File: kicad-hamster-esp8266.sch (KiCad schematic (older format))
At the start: 16 parts

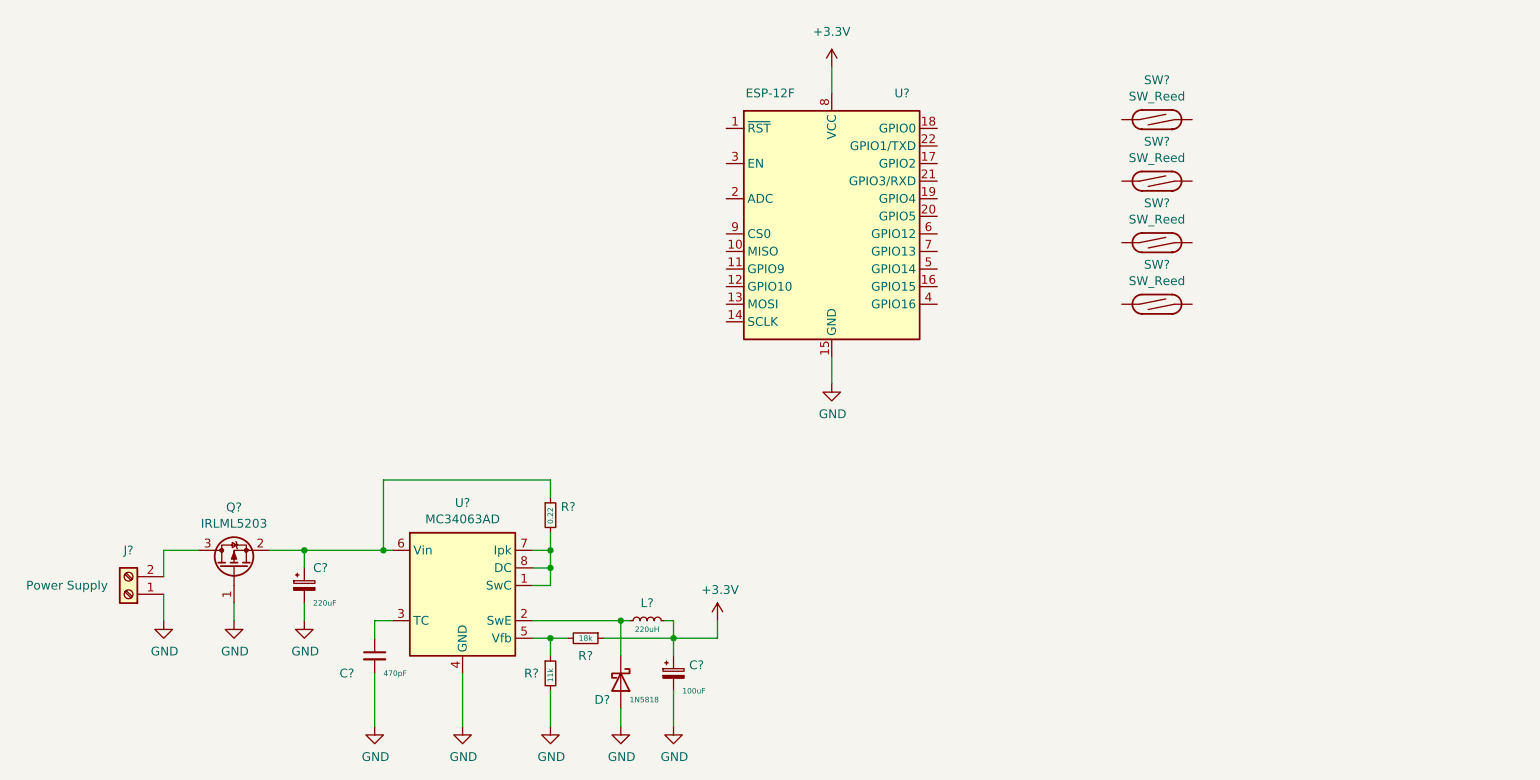
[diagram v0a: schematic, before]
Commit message: hamster v2 esp8266: flash/reset circuitry
Draw flash/reset/enable circuitry including control pins and
specific gpio pins.

Signed-off-by: Sergey Matyukevich <geomatsi@gmail.com>
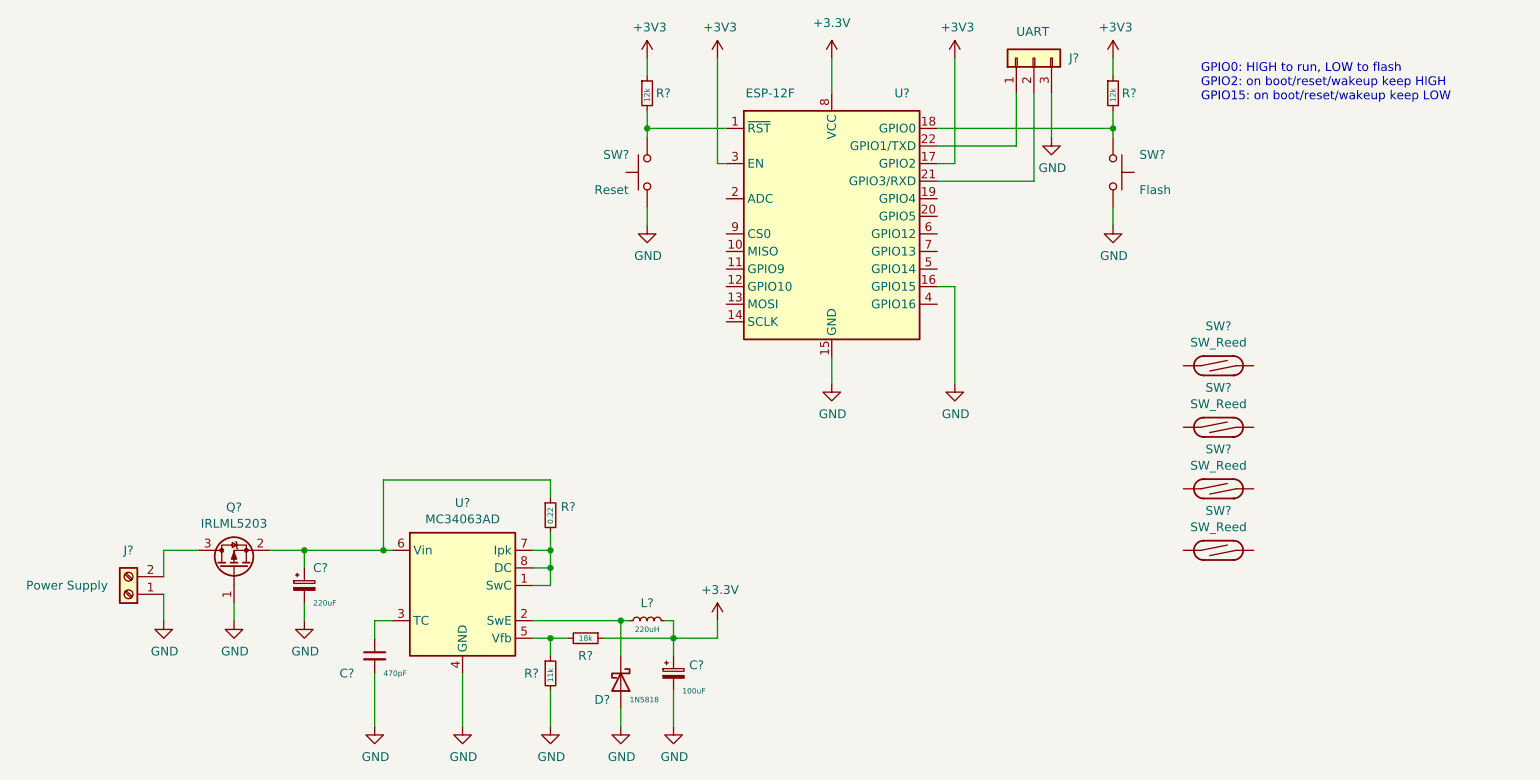
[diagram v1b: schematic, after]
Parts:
- added J?: UART, symbol Connector_Generic:Conn_01x03
- added R? (x2): 12k, symbol Device:R_Small
- added SW?: Flash, symbol Switch:SW_Push
- added SW?: Reset, symbol Switch:SW_Push
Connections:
- net +3V3: now also U?.17 (GPIO2), U?.3 (EN), R?.1, R?.1
- net GND: now also U?.16 (GPIO15), J?.3 (Pin_3), SW?.1, SW?.2
- net at U?.1 (~RST): now also R?.2, SW?.2
- net at U?.18 (GPIO0): now also R?.2, SW?.1
- net at U?.21 (GPIO3/RXD): now also J?.2 (Pin_2)
- net at U?.22 (GPIO1/TXD): now also J?.1 (Pin_1)
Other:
- note added: "GPIO0: HIGH to run, LOW to flash\nGPIO2: on boot/reset/wakeup keep HIGH\nGPIO15: on boot/reset/wakeup keep LOW"
- moved on the sheet: SW?

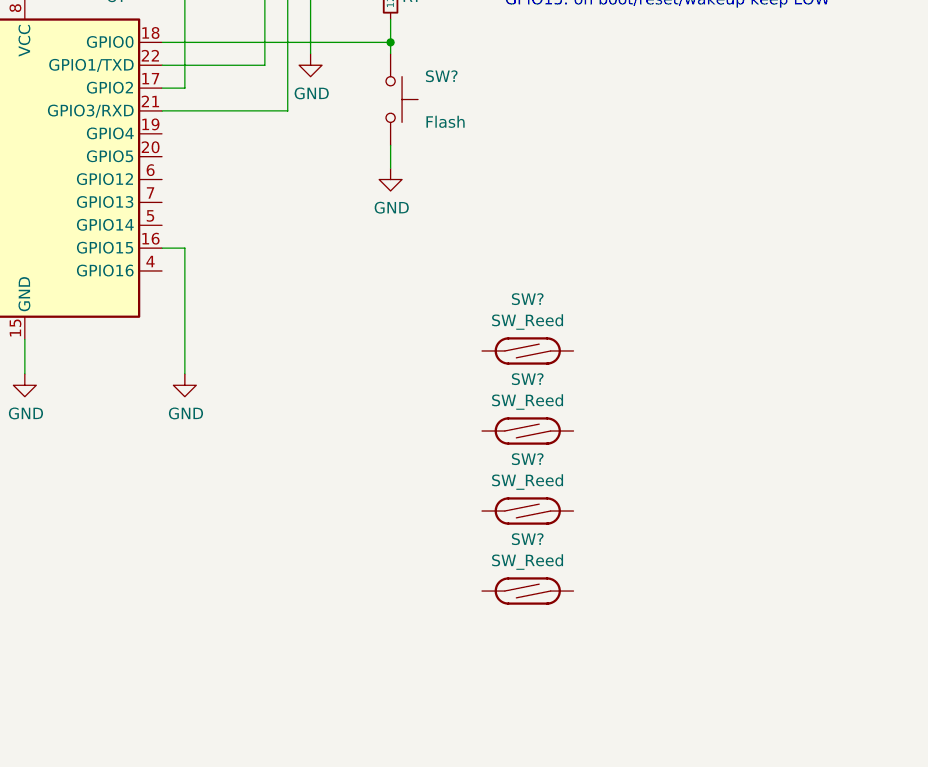
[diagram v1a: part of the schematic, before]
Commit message: hamster v2 esp8266: reed switch circuitry
Draw reed switch circuitry

Signed-off-by: Sergey Matyukevich <geomatsi@gmail.com>
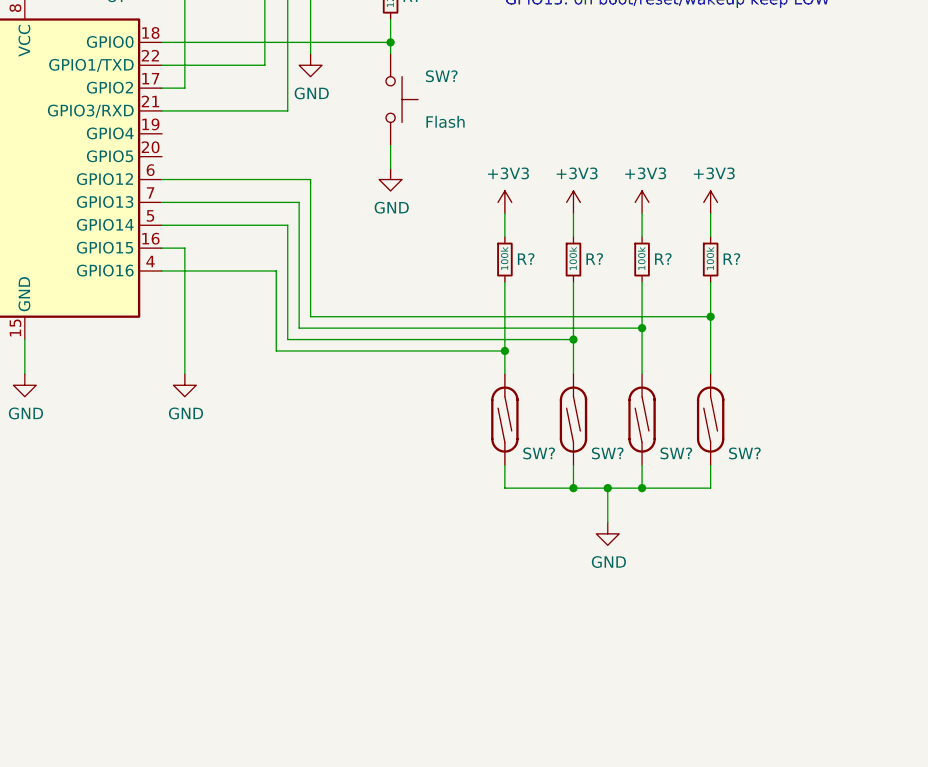
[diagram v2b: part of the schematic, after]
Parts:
- added R? (x4): 100k, symbol Device:R_Small
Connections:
- net +3V3: now also R?.1, R?.1, R?.1, R?.1
- net GND: now also SW?.1, SW?.1, SW?.1, SW?.1
- net at U?.4 (GPIO16): now also SW?.2, R?.2
- net at U?.5 (GPIO14): now also SW?.2, R?.2
- net at U?.6 (GPIO12): now also SW?.2, R?.2
- net at U?.7 (GPIO13): now also SW?.2, R?.2
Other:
- moved on the sheet: SW?
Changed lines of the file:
@@
 L Switch:SW_Reed SW?
 U 1 1 5F0BB0DF
-P 7700 5100
-F 0 "SW?" H 7700 5325 50  0000 C CNN
-F 1 "SW_Reed" H 7700 5232 50  0000 C CNN
-F 2 "" H 7700 5100 50  0001 C CNN
-F 3 "~" H 7700 5100 50  0001 C CNN
-	1    7700 5100
-	1    0    0    -1
+P 8500 4350
+F 0 "SW?" V 8350 4200 50  0000 C CNN
+F 1 "SW_Reed" H 8500 4482 50  0001 C CNN
+F 2 "" H 8500 4350 50  0001 C CNN
+F 3 "~" H 8500 4350 50  0001 C CNN
+	1    8500 4350
+	0    -1   -1   0
 $EndComp
 $Comp
 L Switch:SW_Reed SW?
 U 1 1 5F0BBD95
-P 7700 4750
-F 0 "SW?" H 7700 4975 50  0000 C CNN
-F 1 "SW_Reed" H 7700 4882 50  0000 C CNN
-F 2 "" H 7700 4750 50  0001 C CNN
-F 3 "~" H 7700 4750 50  0001 C CNN
-	1    7700 4750
-	1    0    0    -1
+P 8200 4350
+F 0 "SW?" V 8050 4200 50  0000 C CNN
+F 1 "SW_Reed" H 8200 4482 50  0001 C CNN
+F 2 "" H 8200 4350 50  0001 C CNN
+F 3 "~" H 8200 4350 50  0001 C CNN
+	1    8200 4350
+	0    -1   -1   0
 $EndComp
 $Comp
 L Switch:SW_Reed SW?
 U 1 1 5F0BC4C3
-P 7700 4400
-F 0 "SW?" H 7700 4625 50  0000 C CNN
-F 1 "SW_Reed" H 7700 4532 50  0000 C CNN
-F 2 "" H 7700 4400 50  0001 C CNN
-F 3 "~" H 7700 4400 50  0001 C CNN
-	1    7700 4400
-	1    0    0    -1
+P 7900 4350
+F 0 "SW?" V 7750 4200 50  0000 C CNN
+F 1 "SW_Reed" H 7900 4482 50  0001 C CNN
+F 2 "" H 7900 4350 50  0001 C CNN
+F 3 "~" H 7900 4350 50  0001 C CNN
+	1    7900 4350
+	0    -1   -1   0
 $EndComp
 $Comp
 L Switch:SW_Reed SW?
 U 1 1 5F0BCC12
-P 7700 4050
-F 0 "SW?" H 7700 4275 50  0000 C CNN
-F 1 "SW_Reed" H 7700 4182 50  0000 C CNN
-F 2 "" H 7700 4050 50  0001 C CNN
-F 3 "~" H 7700 4050 50  0001 C CNN
-	1    7700 4050
-	1    0    0    -1
+P 7600 4350
+F 0 "SW?" V 7450 4200 50  0000 C CNN
+F 1 "SW_Reed" H 7600 4482 50  0001 C CNN
+F 2 "" H 7600 4350 50  0001 C CNN
+F 3 "~" H 7600 4350 50  0001 C CNN
+	1    7600 4350
+	0    -1   -1   0
 $EndComp
 $Comp
@@
 Wire Wire Line
 	4850 2900 4850 2300
+$Comp
+L power:+3V3 #PWR?
+U 1 1 5F135AC7
+P 7900 3450
+F 0 "#PWR?" H 7900 3300 50  0001 C CNN
+F 1 "+3V3" H 7915 3625 50  0000 C CNN
+F 2 "" H 7900 3450 50  0001 C CNN
+F 3 "" H 7900 3450 50  0001 C CNN
+	1    7900 3450
+	1    0    0    -1
+$EndComp
+$Comp
+L power:GND #PWR?
+U 1 1 5F136815
+P 8050 4800
+F 0 "#PWR?" H 8050 4550 50  0001 C CNN
+F 1 "GND" H 8055 4625 50  0000 C CNN
+F 2 "" H 8050 4800 50  0001 C CNN
+F 3 "" H 8050 4800 50  0001 C CNN
+	1    8050 4800
+	1    0    0    -1
+$EndComp
+$Comp
+L Device:R_Small R?
+U 1 1 5F1388C7
+P 7900 3650
+F 0 "R?" H 7950 3650 50  0000 L CNN
+F 1 "100k" V 7900 3600 31  0000 L CNN
+F 2 "" H 7900 3650 50  0001 C CNN
+F 3 "~" H 7900 3650 50  0001 C CNN
+	1    7900 3650
+	1    0    0    -1
+$EndComp
+Wire Wire Line
+	7900 4550 7900 4650
+Wire Wire Line
+	8200 4650 8200 4550
+Wire Wire Line
+	8200 4650 8500 4650
+Wire Wire Line
+	8500 4650 8500 4550
+Wire Wire Line
+	7900 4150 7900 4000
+Wire Wire Line
+	8200 4150 8200 3950
+Wire Wire Line
+	8500 4150 8500 3900
+Wire Wire Line
+	7900 3450 7900 3550
+Wire Wire Line
+	7900 4650 8050 4650
+Connection ~ 7900 4650
+Connection ~ 8200 4650
+Wire Wire Line
+	8050 4800 8050 4650
+Connection ~ 8050 4650
+Wire Wire Line
+	8050 4650 8200 4650
+Wire Wire Line
+	7600 4650 7900 4650
+Wire Wire Line
+	7600 4550 7600 4650
+Wire Wire Line
+	6100 3300 6750 3300
+Wire Wire Line
+	6750 3300 6750 3900
+Wire Wire Line
+	6750 3900 8500 3900
+Wire Wire Line
+	6100 3400 6700 3400
+Wire Wire Line
+	6700 3400 6700 3950
+Wire Wire Line
+	6700 3950 8200 3950
+Wire Wire Line
+	6100 3500 6650 3500
+Wire Wire Line
+	6650 3500 6650 4000
+Wire Wire Line
+	6650 4000 7900 4000
+Wire Wire Line
+	6100 3700 6600 3700
+Wire Wire Line
+	6600 3700 6600 4050
+Wire Wire Line
+	6600 4050 7600 4050
+Wire Wire Line
+	7600 4050 7600 4150
+$Comp
+L power:+3V3 #PWR?
+U 1 1 5F1A0238
+P 8200 3450
+F 0 "#PWR?" H 8200 3300 50  0001 C CNN
+F 1 "+3V3" H 8215 3625 50  0000 C CNN
+F 2 "" H 8200 3450 50  0001 C CNN
+F 3 "" H 8200 3450 50  0001 C CNN
+	1    8200 3450
+	1    0    0    -1
+$EndComp
+$Comp
+L Device:R_Small R?
+U 1 1 5F1A023E
+P 8200 3650
+F 0 "R?" H 8250 3650 50  0000 L CNN
+F 1 "100k" V 8200 3600 31  0000 L CNN
+F 2 "" H 8200 3650 50  0001 C CNN
+F 3 "~" H 8200 3650 50  0001 C CNN
+	1    8200 3650
+	1    0    0    -1
+$EndComp
+Wire Wire Line
+	8200 3450 8200 3550
+$Comp
+L power:+3V3 #PWR?
+U 1 1 5F1A2592
+P 8500 3450
+F 0 "#PWR?" H 8500 3300 50  0001 C CNN
+F 1 "+3V3" H 8515 3625 50  0000 C CNN
+F 2 "" H 8500 3450 50  0001 C CNN
+F 3 "" H 8500 3450 50  0001 C CNN
+	1    8500 3450
+	1    0    0    -1
+$EndComp
+$Comp
+L Device:R_Small R?
+U 1 1 5F1A2598
+P 8500 3650
+F 0 "R?" H 8550 3650 50  0000 L CNN
+F 1 "100k" V 8500 3600 31  0000 L CNN
+F 2 "" H 8500 3650 50  0001 C CNN
+F 3 "~" H 8500 3650 50  0001 C CNN
+	1    8500 3650
+	1    0    0    -1
+$EndComp
+Wire Wire Line
+	8500 3450 8500 3550
+$Comp
+L power:+3V3 #PWR?
+U 1 1 5F1A4EF5
+P 7600 3450
+F 0 "#PWR?" H 7600 3300 50  0001 C CNN
+F 1 "+3V3" H 7615 3625 50  0000 C CNN
+F 2 "" H 7600 3450 50  0001 C CNN
+F 3 "" H 7600 3450 50  0001 C CNN
+	1    7600 3450
+	1    0    0    -1
+$EndComp
+$Comp
+L Device:R_Small R?
+U 1 1 5F1A4EFB
+P 7600 3650
+F 0 "R?" H 7650 3650 50  0000 L CNN
+F 1 "100k" V 7600 3600 31  0000 L CNN
+F 2 "" H 7600 3650 50  0001 C CNN
+F 3 "~" H 7600 3650 50  0001 C CNN
+	1    7600 3650
+	1    0    0    -1
+$EndComp
+Wire Wire Line
+	7600 3450 7600 3550
+Wire Wire Line
+	7600 4050 7600 3750
+Connection ~ 7600 4050
+Wire Wire Line
+	7900 3750 7900 4000
+Connection ~ 7900 4000
+Wire Wire Line
+	8200 3950 8200 3750
+Connection ~ 8200 3950
+Wire Wire Line
+	8500 3900 8500 3750
+Connection ~ 8500 3900
 $EndSCHEMATC

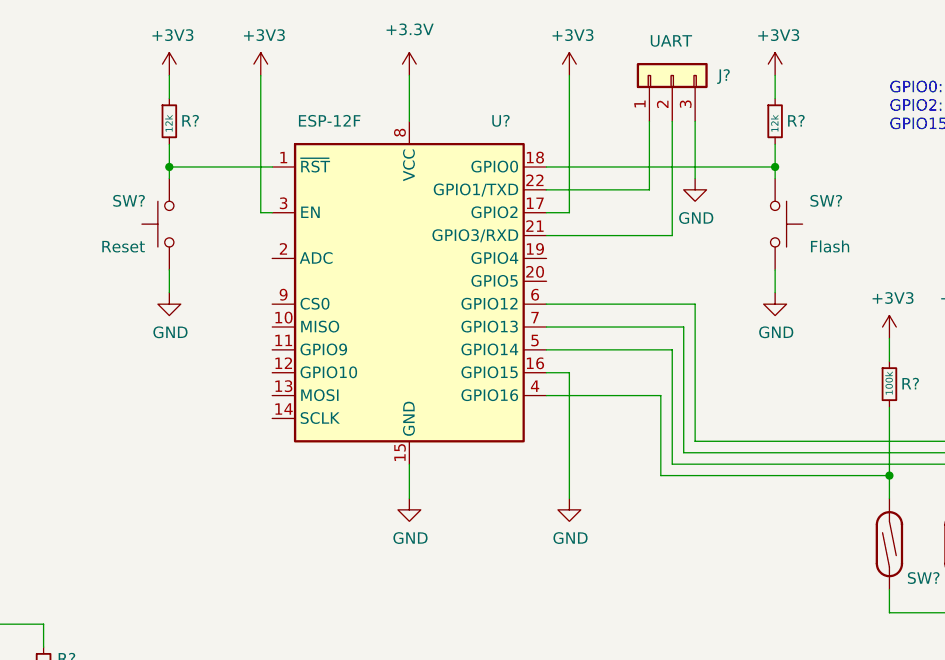
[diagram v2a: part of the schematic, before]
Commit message: hamster v2 esp8266: add pull-ups and pull-downs
Add pull up/down resistors for major ESP pins based
on experiments with prototype board.

Signed-off-by: Sergey Matyukevich <geomatsi@gmail.com>
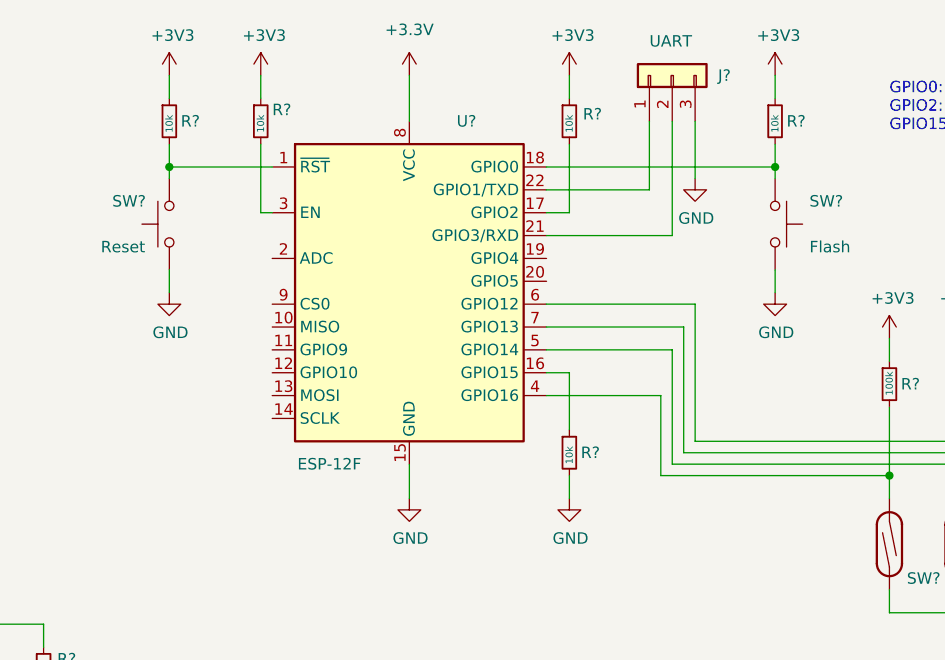
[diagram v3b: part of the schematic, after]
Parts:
- added R? (x3): 10k, symbol Device:R_Small
- R? (x2): value 12k -> 10k
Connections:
- net +3V3: now also R?.1, R?.1; no longer U?.17 (GPIO2), U?.3 (EN)
- net GND: now also R?.2; no longer U?.16 (GPIO15)
- new net: R?.1, U?.16 (GPIO15)
- new net: R?.2, U?.17 (GPIO2)
- new net: R?.2, U?.3 (EN)
